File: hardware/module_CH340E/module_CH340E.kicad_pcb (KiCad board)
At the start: 2 copper layers, 20.1 x 16.7 mm, 18 parts, among them J1 USB-ID, J2 FTDI_PINS_1X06_input, U1 MCP1702-CB, U2 CH340E

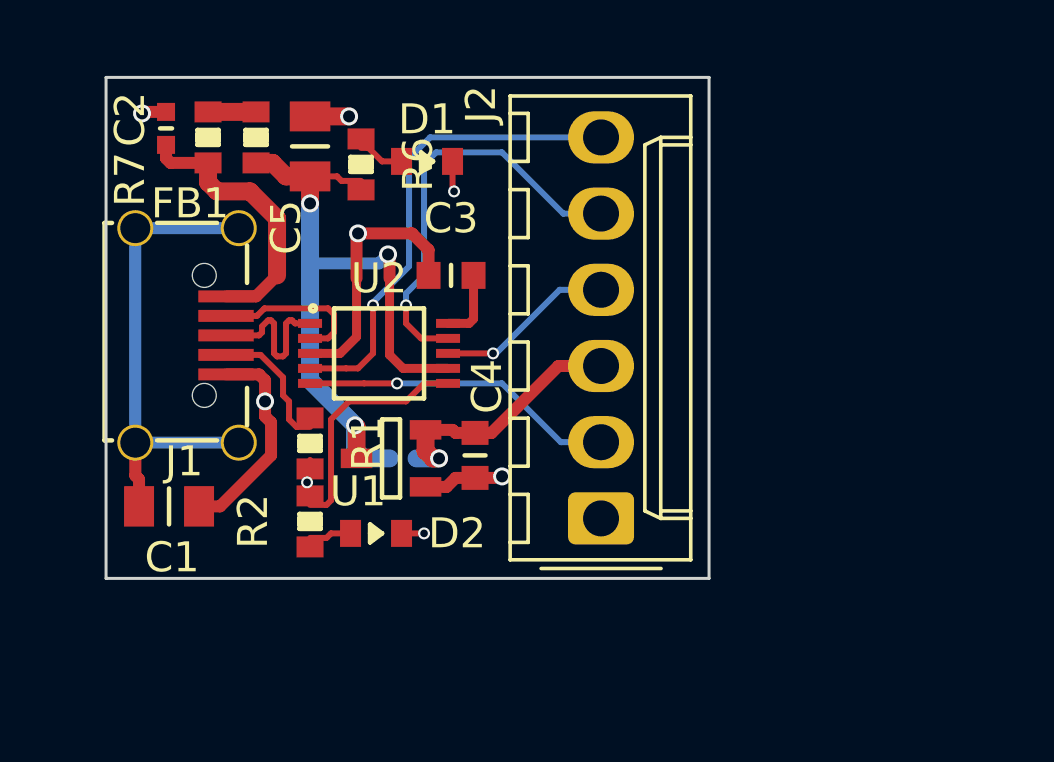
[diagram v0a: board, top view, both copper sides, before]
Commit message: optimized superflous components, WIP PCB layout
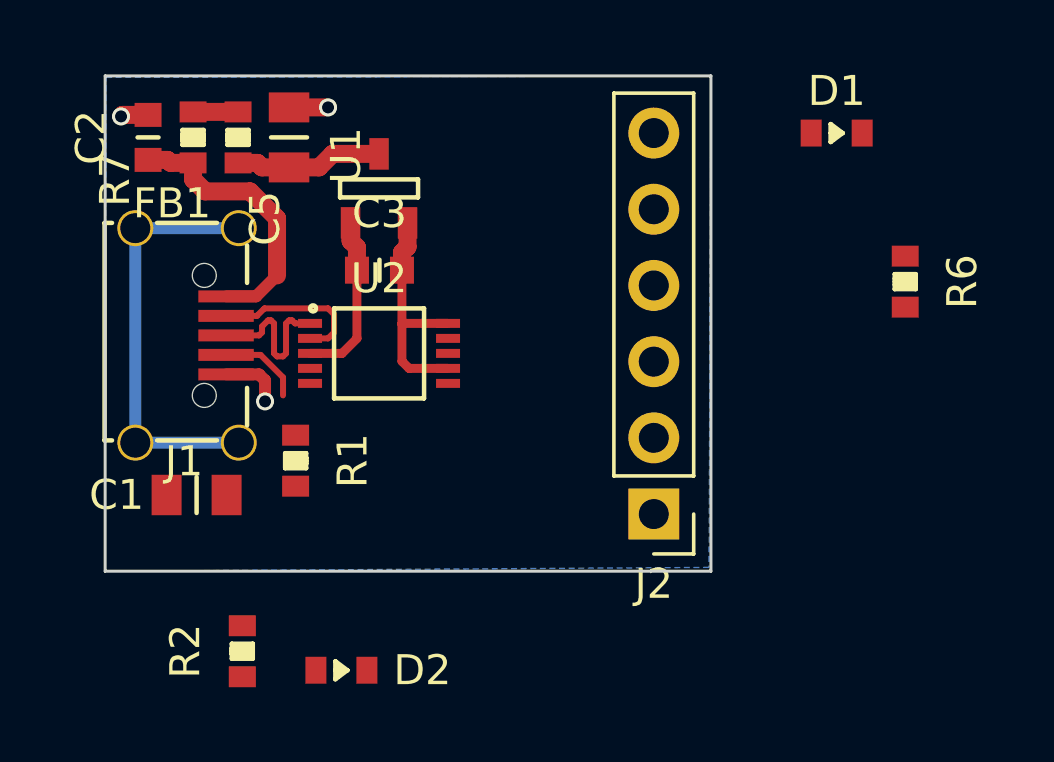
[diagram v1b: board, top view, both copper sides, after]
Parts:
- removed C4: 1u, SquantorRcl:C_0603
- C2: footprint SquantorRcl:C_0402 -> SquantorRcl:C_0603
- J2: footprint SquantorConnectorsNamed:Molex_KK-254_AE-6410-06A_1x06_P2.54mm_Vertical_FTDI_UART -> Connector_PinHeader_2.54mm:PinHeader_1x06_P2.54mm_Vertical
- N2: value 20200607 -> 20200608
- moved R6 18.6 mm to (167.6, 89.4)
- moved D1 13.7 mm to (165.4, 84.5)
- moved U1 9.01 mm to (150.1, 86.3), turned to 0 degrees
- moved R2 4.88 mm to (145.5, 101.7)
- moved D2 4.71 mm to (148.8, 102.4)
- moved C3 2.39 mm to (150.1, 89.0)
- moved J2 1.76 mm to (159.3, 97.2), turned to 180 degrees
- moved C1 0.99 mm to (144.0, 96.5)
- moved C5 0.76 mm to (147.1, 84.6)
- moved R1 0.75 mm to (147.3, 95.4)
- moved C2 0.67 mm to (142.4, 84.6)
- moved FB1 0.60 mm to (145.4, 84.6)
- moved R7 0.50 mm to (143.9, 84.6)
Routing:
- net /VDD: track 24.1 -> 4.95 mm, vias 3 -> 0
- net /RTSO: track 16.0 -> 0.00 mm, vias 1 -> 0
- net /RXI: track 14.1 -> 0.00 mm, vias 1 -> 0
- net /VSS: track 23.1 -> 10.0 mm, vias 8 -> 3
- net /CTSI: track 10.5 -> 0.00 mm, vias 1 -> 0
- net /VDDCONN: track 8.82 -> 0.00 mm, vias 1 -> 0
- net /ACT: track 7.86 -> 0.00 mm
- net /TXO: track 5.98 -> 0.00 mm, vias 1 -> 0
- net /V3: track 2.36 -> 7.87 mm
- net Net-(C1-Pad1): track 16.2 -> 14.1 mm
- net Net-(J1-Pad4): track 4.50 -> 2.81 mm
- net Net-(D1-Pad2): track 1.54 -> 0.00 mm
- net Net-(D2-Pad2): track 1.41 -> 0.00 mm
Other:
- board size 20.1 x 16.7 mm -> 20.2 x 16.5 mm

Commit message: minor changes
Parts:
- moved R6 14.5 mm to (153.4, 86.5), turned to 0 degrees
- moved D1 12.0 mm to (153.4, 85.0)
- moved R2 10.5 mm to (153.4, 94.7), turned to 0 degrees
- moved D2 7.66 mm to (153.4, 96.2)
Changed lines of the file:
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@@
   )
   (module SquantorRcl:R_0603_hand (layer F.Cu)
-    (at 167.64 89.408 270)
+    (at 153.4 86.5)
     (descr "Resistor SMD 0603, reflow soldering, Vishay (see dcrcw.pdf)")
     (tags "resistor 0603")
     (attr smd)
-    (fp_text reference R6 (at 0 -1.9 90) (layer F.SilkS)
-      (effects (font (size 1 1) (thickness 0.15)))
-    )
-    (fp_text value 1K (at 0 1.9 90) (layer F.Fab)
+    (fp_text reference R6 (at 0 -1.9) (layer F.SilkS)
+      (effects (font (size 1 1) (thickness 0.15)))
+    )
+    (fp_text value 1K (at 0 1.9) (layer F.Fab)
       (effects (font (size 1 1) (thickness 0.15)))
     )
@@
     (fp_line (start 0.8 0.4) (end -0.8 0.4) (layer F.Fab) (width 0.1))
     (fp_line (start -0.8 0.4) (end -0.8 -0.4) (layer F.Fab) (width 0.1))
-    (pad 2 smd rect (at 0.85 0 270) (size 0.7 0.9) (layers F.Cu F.Paste F.Mask)
+    (pad 2 smd rect (at 0.85 0) (size 0.7 0.9) (layers F.Cu F.Paste F.Mask)
       (net 4 /VDD))
-    (pad 1 smd rect (at -0.85 0 270) (size 0.7 0.9) (layers F.Cu F.Paste F.Mask)
+    (pad 1 smd rect (at -0.85 0) (size 0.7 0.9) (layers F.Cu F.Paste F.Mask)
       (net 12 "Net-(D1-Pad2)"))
     (model ${KISYS3DMOD}/Resistor_SMD.3dshapes/R_0603_1608Metric.step
@@
   )
   (module SquantorRcl:R_0603_hand (layer F.Cu)
-    (at 145.542 101.727 90)
+    (at 153.4 94.7)
     (descr "Resistor SMD 0603, reflow soldering, Vishay (see dcrcw.pdf)")
     (tags "resistor 0603")
     (attr smd)
-    (fp_text reference R2 (at 0 -1.9 90) (layer F.SilkS)
-      (effects (font (size 1 1) (thickness 0.15)))
-    )
-    (fp_text value 1K (at 0 1.9 90) (layer F.Fab)
+    (fp_text reference R2 (at 0 -1.9) (layer F.SilkS)
+      (effects (font (size 1 1) (thickness 0.15)))
+    )
+    (fp_text value 1K (at 0 1.9) (layer F.Fab)
       (effects (font (size 1 1) (thickness 0.15)))
     )
@@
     (fp_line (start 0.8 0.4) (end -0.8 0.4) (layer F.Fab) (width 0.1))
     (fp_line (start -0.8 0.4) (end -0.8 -0.4) (layer F.Fab) (width 0.1))
-    (pad 2 smd rect (at 0.85 0 90) (size 0.7 0.9) (layers F.Cu F.Paste F.Mask)
+    (pad 2 smd rect (at 0.85 0) (size 0.7 0.9) (layers F.Cu F.Paste F.Mask)
       (net 15 /ACT))
-    (pad 1 smd rect (at -0.85 0 90) (size 0.7 0.9) (layers F.Cu F.Paste F.Mask)
+    (pad 1 smd rect (at -0.85 0) (size 0.7 0.9) (layers F.Cu F.Paste F.Mask)
       (net 14 "Net-(D2-Pad2)"))
     (model ${KISYS3DMOD}/Resistor_SMD.3dshapes/R_0603_1608Metric.step
@@
   )
   (module SquantorDiodes:D_0603_hand (layer F.Cu)
-    (at 165.354 84.455 180)
+    (at 153.4 85 180)
     (descr "Diode SMD 0603, reflow soldering, general purpose")
     (tags "Diode 0603")
@@
   )
   (module SquantorDiodes:D_0603_hand (layer F.Cu)
-    (at 148.844 102.362 180)
+    (at 153.4 96.2 180)
     (descr "Diode SMD 0603, reflow soldering, general purpose")
     (tags "Diode 0603")

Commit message: WIP layout, silk placement
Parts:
- moved D2 1.12 mm to (153.9, 97.2)
- moved D1 1.08 mm to (153.8, 84.0)
- moved R2 1.03 mm to (153.9, 95.6)
- moved R6 0.98 mm to (153.8, 85.6)
- moved C3 0.07 mm to (150.1, 89.1)
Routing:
- net /VDD: track 4.95 -> 20.7 mm
- net /VSS: track 10.0 -> 12.3 mm, vias 3 -> 5
- net Net-(D1-Pad2): track 0.00 -> 1.60 mm
- added copper zone on F.Cu, net /VDD
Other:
- board text added: "CTS"
- board text added: "RTS"
- board text added: "RX"
- board text added: "TX"
- board text added: "VDD"
- board text added: "VSS"

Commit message: routing completed
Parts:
- moved C1 0.48 mm to (144.0, 97.0)
- moved D1 0.40 mm to (153.8, 84.4)
- moved R6 0.30 mm to (153.8, 85.9)
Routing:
- net /RTSO: track 0.00 -> 16.2 mm, vias 0 -> 1
- net /CTSI: track 0.00 -> 12.2 mm, vias 0 -> 1
- net /RXI: track 0.00 -> 9.31 mm, vias 0 -> 1
- net /TXO: track 0.00 -> 7.80 mm, vias 0 -> 1
- net /VSS: track 12.3 -> 19.8 mm, vias 5 -> 7
- net /ACT: track 0.00 -> 4.30 mm
- net Net-(C1-Pad1): track 14.1 -> 17.1 mm
- net Net-(D2-Pad2): track 0.00 -> 1.60 mm
- net Net-(J1-Pad4): track 2.81 -> 4.31 mm
- net /VDD: track 20.7 -> 19.8 mm
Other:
- board text added: "Activity"
- board text added: "Power"
